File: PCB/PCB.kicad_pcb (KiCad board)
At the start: 2 copper layers, 120 x 60 mm, 62 parts, among them J1 USB_C_Receptacle_USB2.0_16P, J2 Conn_01x15, J3 Conn_01x15, Q2 IRLML2060, SW1 TSA016A2526B, SW2 TSA016A2526B, SW3 TSA016A2526B, U1 RP2040, U2 USBLC6-2SC6, U3 NCP1117ST33T3G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

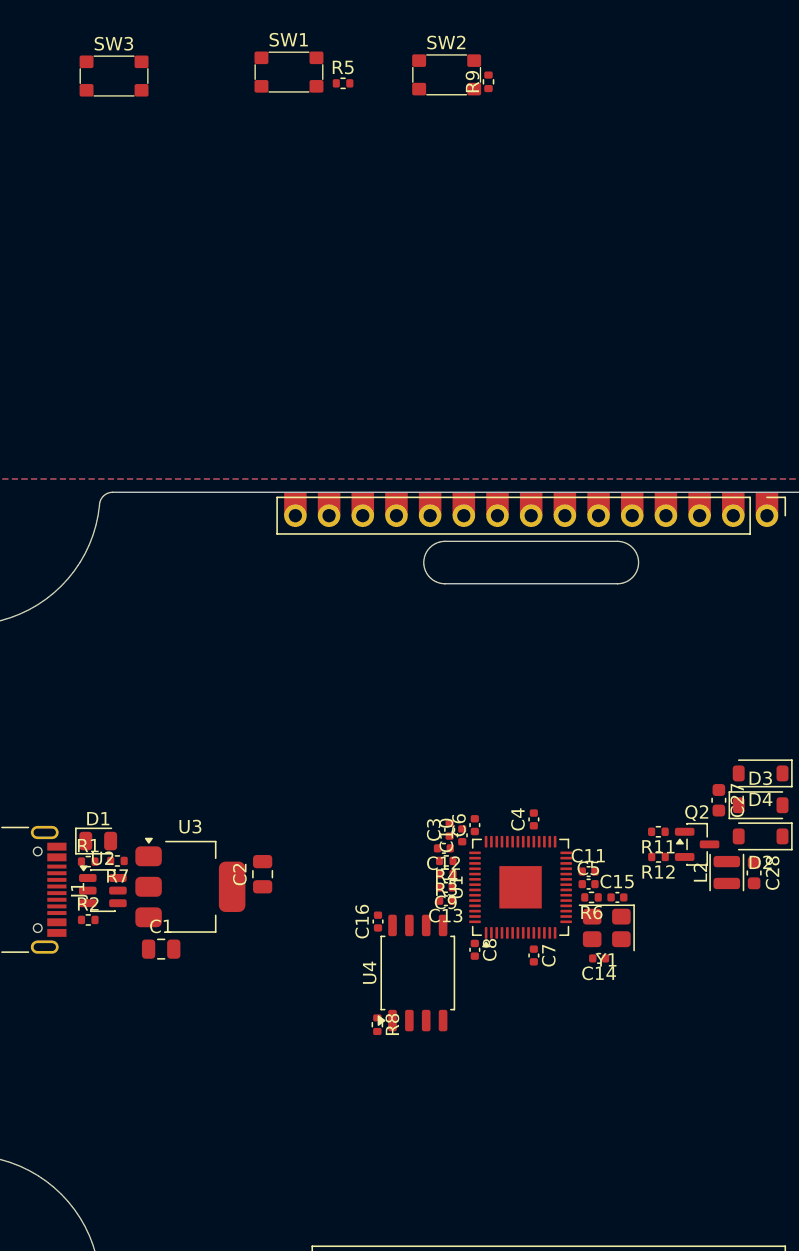
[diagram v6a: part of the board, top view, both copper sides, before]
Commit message: aligned the buttons
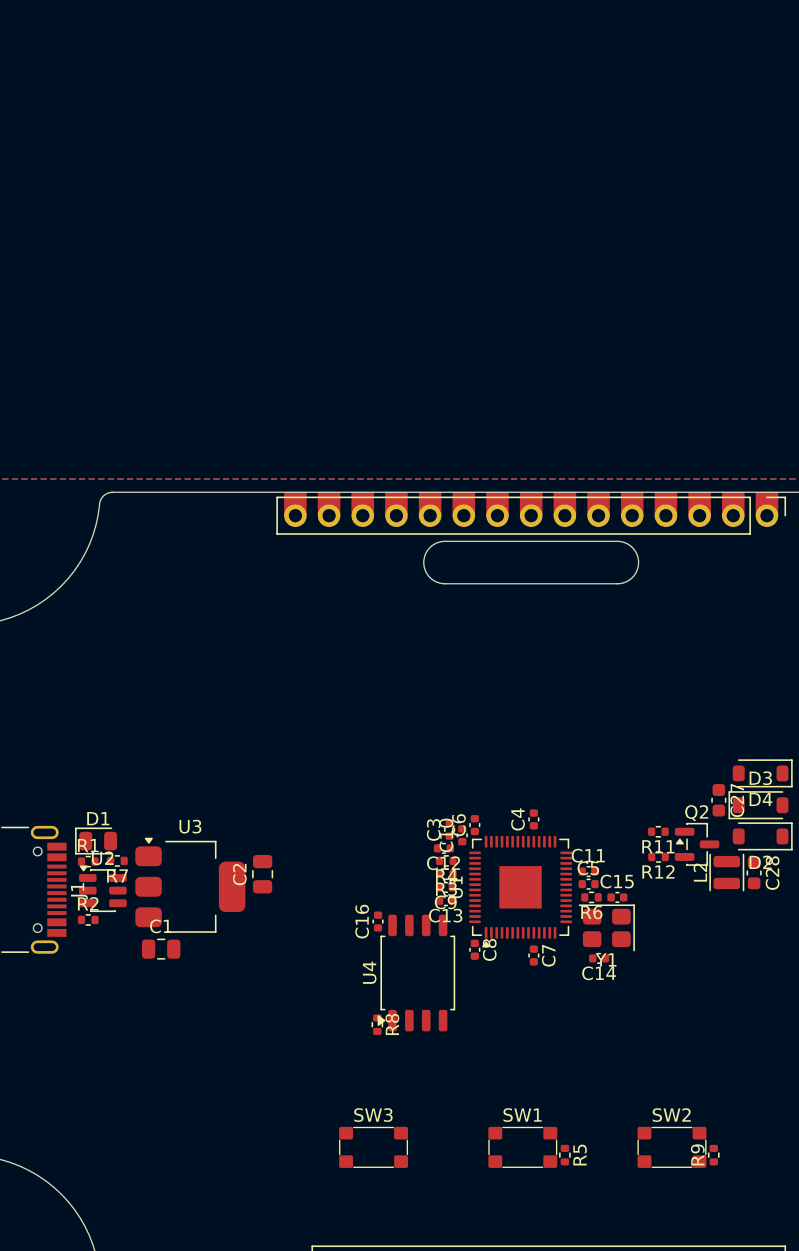
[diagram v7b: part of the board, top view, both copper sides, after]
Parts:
- moved SW3 83.1 mm to (100.6, 144.4)
- moved SW1 83.0 mm to (111.9, 144.4)
- moved R9 82.7 mm to (126.3, 145.0)
- moved SW2 82.6 mm to (123.1, 144.4)
- moved R5 82.5 mm to (115.0, 145.0), turned to -90 degrees
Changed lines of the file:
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@@
 	(footprint "Resistor_SMD:R_0402_1005Metric"
 		(layer "F.Cu")
-		(at 98.315 64.165)
+		(at 115.0425 144.985 -90)
 		(descr "Resistor SMD 0402 (1005 Metric), square (rectangular) end terminal, IPC-7351 nominal, (Body size source: IPC-SM-782 page 72, https://www.pcb-3d.com/wordpress/wp-content/uploads/ipc-sm-782a_amendment_1_and_2.pdf), generated with kicad-footprint-generator")
 		(tags "resistor")
 		(property "Reference" "R5"
-			(at 0 -1.17 0)
+			(at 0 -1.17 90)
 			(layer "F.SilkS")
 			(effects
@@
 		)
 		(property "Value" "10K"
-			(at 0 1.17 0)
+			(at 0 1.17 90)
 			(layer "F.Fab")
 			(effects
@@
 		)
 		(property "Datasheet" "~"
-			(at 0 0 0)
+			(at 0 0 90)
 			(layer "F.Fab")
 			(hide yes)
@@
 		)
 		(property "Description" "Resistor"
-			(at 0 0 0)
+			(at 0 0 90)
 			(layer "F.Fab")
 			(hide yes)
@@
 		(attr smd)
 		(fp_line
-			(start -0.153641 -0.38)
-			(end 0.153641 -0.38)
+			(start -0.153641 0.38)
+			(end 0.153641 0.38)
 			(stroke
 				(width 0.12)
@@
 		)
 		(fp_line
-			(start -0.153641 0.38)
-			(end 0.153641 0.38)
+			(start -0.153641 -0.38)
+			(end 0.153641 -0.38)
 			(stroke
 				(width 0.12)
@@
 		)
 		(fp_line
-			(start -0.93 -0.47)
-			(end 0.93 -0.47)
+			(start -0.93 0.47)
+			(end -0.93 -0.47)
 			(stroke
 				(width 0.05)
@@
 		)
 		(fp_line
-			(start -0.93 0.47)
-			(end -0.93 -0.47)
+			(start 0.93 0.47)
+			(end -0.93 0.47)
 			(stroke
 				(width 0.05)
@@
 		)
 		(fp_line
-			(start 0.93 -0.47)
-			(end 0.93 0.47)
+			(start -0.93 -0.47)
+			(end 0.93 -0.47)
 			(stroke
 				(width 0.05)
@@
 		)
 		(fp_line
-			(start 0.93 0.47)
-			(end -0.93 0.47)
+			(start 0.93 -0.47)
+			(end 0.93 0.47)
 			(stroke
 				(width 0.05)
@@
 		)
 		(fp_line
-			(start -0.525 -0.27)
-			(end 0.525 -0.27)
+			(start -0.525 0.27)
+			(end -0.525 -0.27)
 			(stroke
 				(width 0.1)
@@
 		)
 		(fp_line
-			(start -0.525 0.27)
-			(end -0.525 -0.27)
+			(start 0.525 0.27)
+			(end -0.525 0.27)
 			(stroke
 				(width 0.1)
@@
 		)
 		(fp_line
-			(start 0.525 -0.27)
-			(end 0.525 0.27)
+			(start -0.525 -0.27)
+			(end 0.525 -0.27)
 			(stroke
 				(width 0.1)
@@
 		)
 		(fp_line
-			(start 0.525 0.27)
-			(end -0.525 0.27)
+			(start 0.525 -0.27)
+			(end 0.525 0.27)
 			(stroke
 				(width 0.1)
@@
 		)
 		(fp_text user "${REFERENCE}"
-			(at 0 0 0)
+			(at 0 0 90)
 			(layer "F.Fab")
 			(effects
@@
 		)
 		(pad "1" smd roundrect
-			(at -0.51 0)
+			(at -0.51 0 270)
 			(size 0.54 0.64)
 			(layers "F.Cu" "F.Mask" "F.Paste")
@@
 		)
 		(pad "2" smd roundrect
-			(at 0.51 0)
+			(at 0.51 0 270)
 			(size 0.54 0.64)
 			(layers "F.Cu" "F.Mask" "F.Paste")
@@
 	(footprint "kai's library:SW_Push_SPST_TSA016"
 		(layer "F.Cu")
-		(at 81.045 63.615)
+		(at 100.6125 144.4)
 		(property "Reference" "SW3"
 			(at 0 -2.4 0)
@@
 	(footprint "kai's library:SW_Push_SPST_TSA016"
 		(layer "F.Cu")
-		(at 94.235 63.315)
+		(at 111.8675 144.4)
 		(property "Reference" "SW1"
 			(at 0 -2.4 0)
@@
 	(footprint "Resistor_SMD:R_0402_1005Metric"
 		(layer "F.Cu")
-		(at 109.28 64.05 90)
+		(at 126.2675 144.985 90)
 		(descr "Resistor SMD 0402 (1005 Metric), square (rectangular) end terminal, IPC-7351 nominal, (Body size source: IPC-SM-782 page 72, https://www.pcb-3d.com/wordpress/wp-content/uploads/ipc-sm-782a_amendment_1_and_2.pdf), generated with kicad-footprint-generator")
 		(tags "resistor")
@@
 	(footprint "kai's library:SW_Push_SPST_TSA016"
 		(layer "F.Cu")
-		(at 106.125 63.525)
+		(at 123.1175 144.4)
 		(property "Reference" "SW2"
 			(at 0 -2.4 0)
@@
 	)
 	(group ""
+		(members "1a6b6959-9183-425e-9c74-a4a69f2bac83" "a457b9a4-d123-43a2-852c-0de9eb0b910d")
+	)
+	(group ""
+		(members "36eb042a-1c93-4d81-a2b3-aae0d796f4dd" "395dfa78-b875-48de-9473-7d3c7dc5c6ed"
+			"f056d585-3bf3-4372-981c-c969d658ac61"
+		)
+	)
+	(group ""
+		(members "ac6c7a75-b99a-4f55-8c30-232e26e992e5" "c5aaef6b-7002-4f42-9dc3-2df0d3db1f72")
+	)
+	(group ""

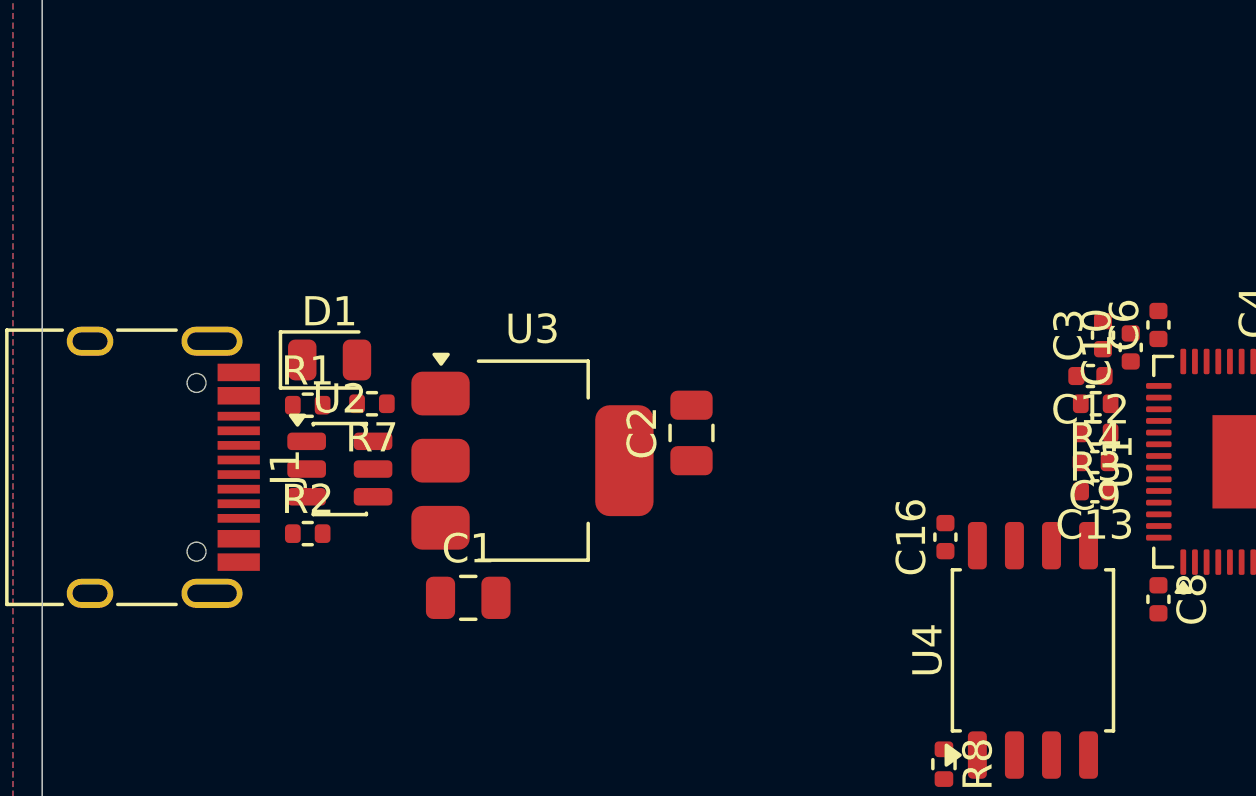
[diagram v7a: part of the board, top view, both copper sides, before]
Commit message: adding the tape keepout, re-aligning the LDO and LED
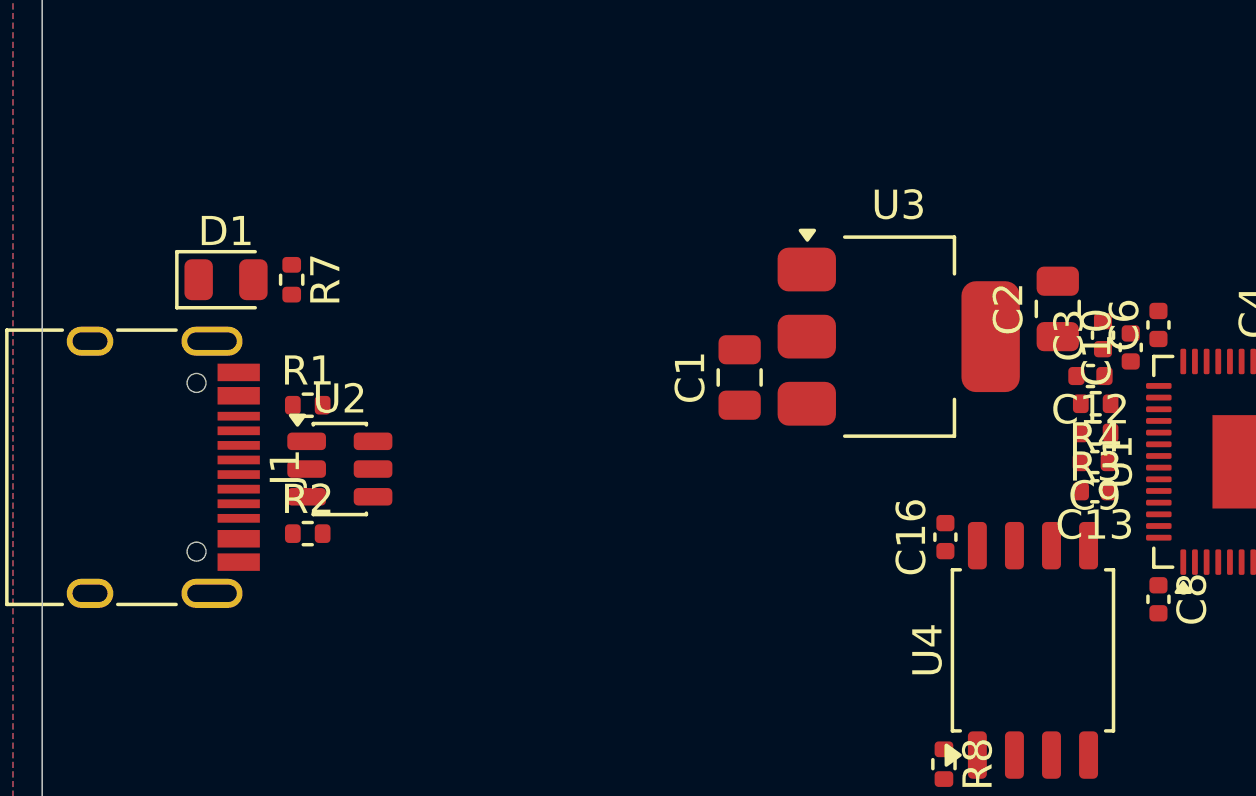
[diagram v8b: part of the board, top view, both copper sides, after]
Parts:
- moved C2 13.3 mm to (104.8, 119.5)
- moved U3 13.3 mm to (99.3, 120.5)
- moved C1 12.0 mm to (93.9, 121.9), turned to 90 degrees
- moved R7 5.06 mm to (78.5, 118.5), turned to -90 degrees
- moved D1 4.49 mm to (76.3, 118.5)
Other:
- board text added: "TAPE KEEPOUT"
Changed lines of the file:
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@@
 	(footprint "LED_SMD:LED_0805_2012Metric"
 		(layer "F.Cu")
-		(at 79.85 121.3)
+		(at 76.3 118.55)
 		(descr "LED SMD 0805 (2012 Metric), square (rectangular) end terminal, IPC-7351 nominal, (Body size source: https://docs.google.com/spreadsheets/d/1BsfQQcO9C6DZCsRaXUlFlo91Tg2WpOkGARC1WS5S8t0/edit?usp=sharing), generated with kicad-footprint-generator")
 		(tags "LED")
@@
 	(footprint "Package_TO_SOT_SMD:SOT-223-3_TabPin2"
 		(layer "F.Cu")
-		(at 86.8 124.75)
+		(at 99.35 120.5)
 		(descr "module CMS SOT223 4 pins")
 		(tags "CMS SOT")
@@
 	(footprint "Resistor_SMD:R_0402_1005Metric"
 		(layer "F.Cu")
-		(at 81.3 122.8 180)
+		(at 78.55 118.55 -90)
 		(descr "Resistor SMD 0402 (1005 Metric), square (rectangular) end terminal, IPC-7351 nominal, (Body size source: IPC-SM-782 page 72, https://www.pcb-3d.com/wordpress/wp-content/uploads/ipc-sm-782a_amendment_1_and_2.pdf), generated with kicad-footprint-generator")
 		(tags "resistor")
 		(property "Reference" "R7"
-			(at 0 -1.17 0)
+			(at 0 -1.17 90)
 			(layer "F.SilkS")
 			(effects
@@
 		)
 		(property "Value" "220"
-			(at 0 1.17 0)
+			(at 0 1.17 90)
 			(layer "F.Fab")
 			(effects
@@
 		)
 		(property "Datasheet" "~"
-			(at 0 0 0)
+			(at 0 0 90)
 			(layer "F.Fab")
 			(hide yes)
@@
 		)
 		(property "Description" "Resistor"
-			(at 0 0 0)
+			(at 0 0 90)
 			(layer "F.Fab")
 			(hide yes)
@@
 		)
 		(fp_line
-			(start 0.93 0.47)
-			(end -0.93 0.47)
+			(start -0.93 0.47)
+			(end -0.93 -0.47)
 			(stroke
 				(width 0.05)
@@
 		)
 		(fp_line
-			(start 0.93 -0.47)
-			(end 0.93 0.47)
+			(start 0.93 0.47)
+			(end -0.93 0.47)
 			(stroke
 				(width 0.05)
@@
 		)
 		(fp_line
-			(start -0.93 0.47)
-			(end -0.93 -0.47)
+			(start -0.93 -0.47)
+			(end 0.93 -0.47)
 			(stroke
 				(width 0.05)
@@
 		)
 		(fp_line
-			(start -0.93 -0.47)
-			(end 0.93 -0.47)
+			(start 0.93 -0.47)
+			(end 0.93 0.47)
 			(stroke
 				(width 0.05)
@@
 		)
 		(fp_line
-			(start 0.525 0.27)
-			(end -0.525 0.27)
+			(start -0.525 0.27)
+			(end -0.525 -0.27)
 			(stroke
 				(width 0.1)
@@
 		)
 		(fp_line
-			(start 0.525 -0.27)
-			(end 0.525 0.27)
+			(start 0.525 0.27)
+			(end -0.525 0.27)
 			(stroke
 				(width 0.1)
@@
 		)
 		(fp_line
-			(start -0.525 0.27)
-			(end -0.525 -0.27)
+			(start -0.525 -0.27)
+			(end 0.525 -0.27)
 			(stroke
 				(width 0.1)
@@
 		)
 		(fp_line
-			(start -0.525 -0.27)
-			(end 0.525 -0.27)
+			(start 0.525 -0.27)
+			(end 0.525 0.27)
 			(stroke
 				(width 0.1)
@@
 		)
 		(fp_text user "${REFERENCE}"
-			(at 0 0 0)
+			(at 0 0 90)
 			(layer "F.Fab")
 			(effects
@@
 		)
 		(pad "1" smd roundrect
-			(at -0.51 0 180)
+			(at -0.51 0 270)
 			(size 0.54 0.64)
 			(layers "F.Cu" "F.Mask" "F.Paste")
@@
 		)
 		(pad "2" smd roundrect
-			(at 0.51 0 180)
+			(at 0.51 0 270)
 			(size 0.54 0.64)
 			(layers "F.Cu" "F.Mask" "F.Paste")
@@
 	(footprint "Capacitor_SMD:C_0805_2012Metric"
 		(layer "F.Cu")
-		(at 92.25 123.8 90)
+		(at 104.8 119.55 90)
 		(descr "Capacitor SMD 0805 (2012 Metric), square (rectangular) end terminal, IPC-7351 nominal, (Body size source: IPC-SM-782 page 76, https://www.pcb-3d.com/wordpress/wp-content/uploads/ipc-sm-782a_amendment_1_and_2.pdf, https://docs.google.com/spreadsheets/d/1BsfQQcO9C6DZCsRaXUlFlo91Tg2WpOkGARC1WS5S8t0/edit?usp=sharing), generated with kicad-footprint-generator")
 		(tags "capacitor")
@@
 	(footprint "Capacitor_SMD:C_0805_2012Metric"
 		(layer "F.Cu")
-		(at 84.6 129.45)
+		(at 93.9 121.9 90)
 		(descr "Capacitor SMD 0805 (2012 Metric), square (rectangular) end terminal, IPC-7351 nominal, (Body size source: IPC-SM-782 page 76, https://www.pcb-3d.com/wordpress/wp-content/uploads/ipc-sm-782a_amendment_1_and_2.pdf, https://docs.google.com/spreadsheets/d/1BsfQQcO9C6DZCsRaXUlFlo91Tg2WpOkGARC1WS5S8t0/edit?usp=sharing), generated with kicad-footprint-generator")
 		(tags "capacitor")
 		(property "Reference" "C1"
-			(at 0 -1.68 0)
+			(at 0 -1.68 90)
 			(layer "F.SilkS")
 			(effects
@@
 		)
 		(property "Value" "10uF"
-			(at 0 1.68 0)
+			(at 0 1.68 90)
 			(layer "F.Fab")
 			(effects
@@
 		)
 		(property "Datasheet" "~"
-			(at 0 0 0)
+			(at 0 0 90)
 			(layer "F.Fab")
 			(hide yes)
@@
 		)
 		(property "Description" "Unpolarized capacitor"
-			(at 0 0 0)
+			(at 0 0 90)
 			(layer "F.Fab")
 			(hide yes)
@@
 		)
 		(fp_line
-			(start -1.7 -0.98)
-			(end 1.7 -0.98)
+			(start 1.7 -0.98)
+			(end 1.7 0.98)
 			(stroke
 				(width 0.05)
@@
 		)
 		(fp_line
-			(start -1.7 0.98)
-			(end -1.7 -0.98)
+			(start -1.7 -0.98)
+			(end 1.7 -0.98)
 			(stroke
 				(width 0.05)
@@
 		)
 		(fp_line
-			(start 1.7 -0.98)
-			(end 1.7 0.98)
+			(start 1.7 0.98)
+			(end -1.7 0.98)
 			(stroke
 				(width 0.05)
@@
 		)
 		(fp_line
-			(start 1.7 0.98)
-			(end -1.7 0.98)
+			(start -1.7 0.98)
+			(end -1.7 -0.98)
 			(stroke
 				(width 0.05)
@@
 		)
 		(fp_line
-			(start -1 -0.625)
-			(end 1 -0.625)
+			(start 1 -0.625)
+			(end 1 0.625)
 			(stroke
 				(width 0.1)
@@
 		)
 		(fp_line
-			(start -1 0.625)
-			(end -1 -0.625)
+			(start -1 -0.625)
+			(end 1 -0.625)
 			(stroke
 				(width 0.1)
@@
 		)
 		(fp_line
-			(start 1 -0.625)
-			(end 1 0.625)
+			(start 1 0.625)
+			(end -1 0.625)
 			(stroke
 				(width 0.1)
@@
 		)
 		(fp_line
-			(start 1 0.625)
-			(end -1 0.625)
+			(start -1 0.625)
+			(end -1 -0.625)
 			(stroke
 				(width 0.1)
@@
 		)
 		(fp_text user "${REFERENCE}"
-			(at 0 0 0)
+			(at 0 0 90)
 			(layer "F.Fab")
 			(effects
@@
 		)
 		(pad "1" smd roundrect
-			(at -0.95 0)
+			(at -0.95 0 90)
 			(size 1 1.45)
 			(layers "F.Cu" "F.Mask" "F.Paste")
@@
 		)
 		(pad "2" smd roundrect
-			(at 0.95 0)
+			(at 0.95 0 90)
 			(size 1 1.45)
 			(layers "F.Cu" "F.Mask" "F.Paste")
@@
 	)
 	(gr_rect
+		(start 84.2 112.8)
+		(end 91.6 138)
+		(stroke
+			(width 0.1)
+			(type default)
+		)
+		(fill no)
+		(layer "Dwgs.User")
+	)
+	(gr_rect
 		(start 82.456 109.546)
 		(end 142.544 140.25)
@@
 		(layer "Dwgs.User")
 		(effects
+			(font
+				(size 1 1)
+				(thickness 0.15)
+			)
+			(justify left bottom)
+		)
+	)
+	(gr_text "TAPE KEEPOUT"
+		(at 86 124.4 90)
+		(layer "Dwgs.User")
+		(effects
